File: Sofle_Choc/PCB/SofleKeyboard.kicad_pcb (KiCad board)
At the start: 2 copper layers, 143.4 x 111.8 mm, 84 parts, among them J2 4PIN, J3 OLED, P1 i2c_pin, P2 i2c_pin, SW1 SW_PUSH_LED, SW10 SW_PUSH_LED, SW11 SW_PUSH_LED, SW12 SW_PUSH_LED, SW13 SW_PUSH_LED, SW14 SW_PUSH_LED, SW15 SW_PUSH_LED, SW16 SW_PUSH_LED, SW17 SW_PUSH_LED, SW18 SW_PUSH_LED, SW19 SW_PUSH_LED, SW2 SW_PUSH_LED, SW20 SW_PUSH_LED, SW21 SW_PUSH_LED, SW22 SW_PUSH_LED, SW23 SW_PUSH_LED, SW24 SW_PUSH_LED, SW25 Rotary_Encoder_Switch, SW26 SW_PUSH_LED, SW27 SW_PUSH_LED, SW28 SW_PUSH_LED, SW29 SW_PUSH_LED, SW3 SW_PUSH_LED, SW30 SW_PUSH_LED, SW4 SW_PUSH_LED, SW5 SW_PUSH_LED, SW6 SW_PUSH_LED, SW7 SW_PUSH_LED, SW8 SW_PUSH_LED, SW9 SW_PUSH_LED, U1 ProMicro

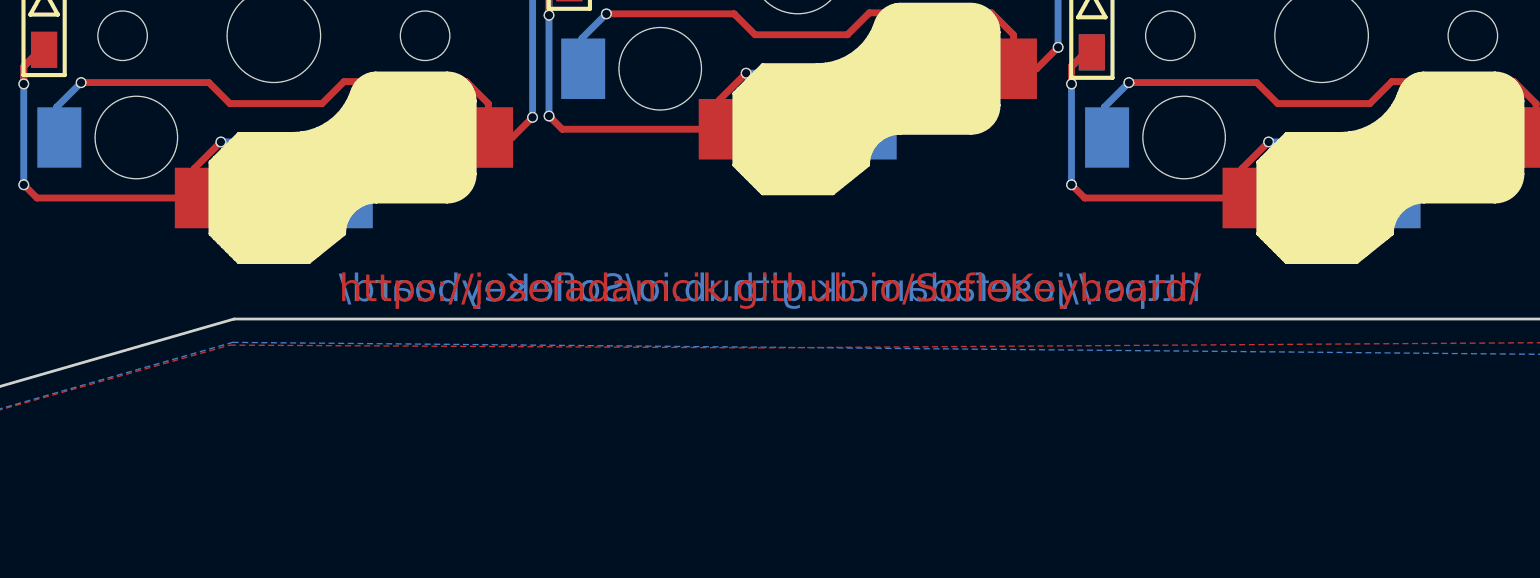
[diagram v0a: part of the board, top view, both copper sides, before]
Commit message: Remove links from copper layer
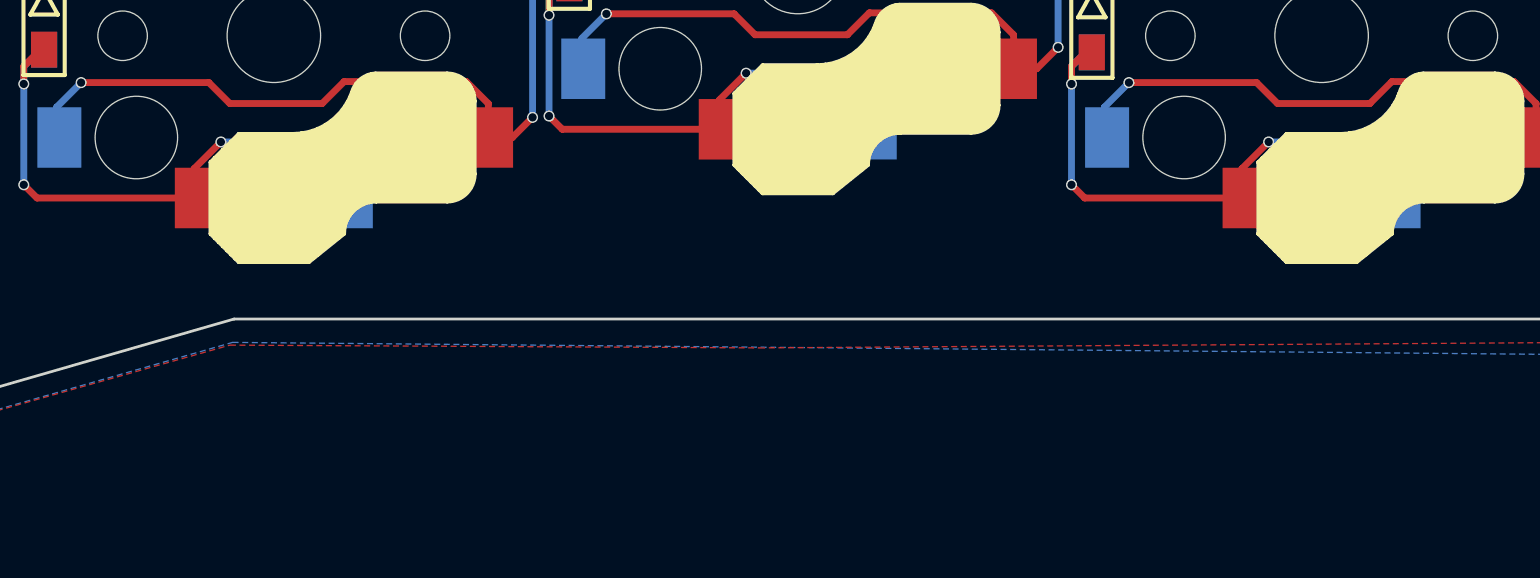
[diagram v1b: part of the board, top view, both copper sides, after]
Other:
- board text removed: "https://josefadamcik.github.io/SofleKeyboard/"
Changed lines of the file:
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@@
-(kicad_pcb (version 20171130) (host pcbnew "(5.1.9-0-10_14)")
+(kicad_pcb (version 20171130) (host pcbnew "(5.1.12-1-10_14)")
   (general
     (thickness 1.6)
-    (drawings 109)
+    (drawings 107)
     (tracks 3233)
     (zones 0)
@@
       (psa4output false)
       (plotreference true)
-      (plotvalue true)
+      (plotvalue false)
       (plotinvisibletext false)
       (padsonsilk false)
@@
       (drillshape 0)
       (scaleselection 1)
-      (outputdirectory "../../Gerbers/Choc_v2/"))
+      (outputdirectory "../../Gerbers/Choc_v2a/"))
   )
   (net 0 "")
@@
   (gr_line (start 92.55 146.2) (end 82.3 128.4) (layer Edge.Cuts) (width 0.1))
   (gr_line (start 225.283881 43.997807) (end 225.370281 44.178672) (layer Edge.Cuts) (width 0.1))
-  (gr_text https://josefadamcik.github.io/SofleKeyboard/ (at 157.64162 132.88464) (layer F.Cu)
-    (effects (font (size 1 1) (thickness 0.15)))
-  )
-  (gr_text https://josefadamcik.github.io/SofleKeyboard/ (at 157.64162 132.88464) (layer B.Cu)
-    (effects (font (size 1 1) (thickness 0.15)) (justify mirror))
-  )
   (gr_text "Sofle Choc v2.1 by Brian Low" (at 201 127.25 21) (layer B.SilkS)
     (effects (font (size 1 1) (thickness 0.2)) (justify mirror))
